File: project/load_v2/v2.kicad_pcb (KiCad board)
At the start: 2 copper layers, 118 parts, among them IC1 ATMEGA328-P, P1 12VAC, P10 relay, P2 NGUON, P3 SAC, P4 12N60C, P5 CONN_01X02, P6 button, P7 UART, P8 FAN, P9 7-seg, Q1 Q_NPN_BCE, Q2 Q_NPN_BCE, Q3 Q_NPN_BCE, SW1 reset, U1 LM7812CT, U2 LM7805CT, U3 ICL7660, U4 TL431, U5 LM324N, U6 LM324N, U7 LM7812CT, Y1 16MHz

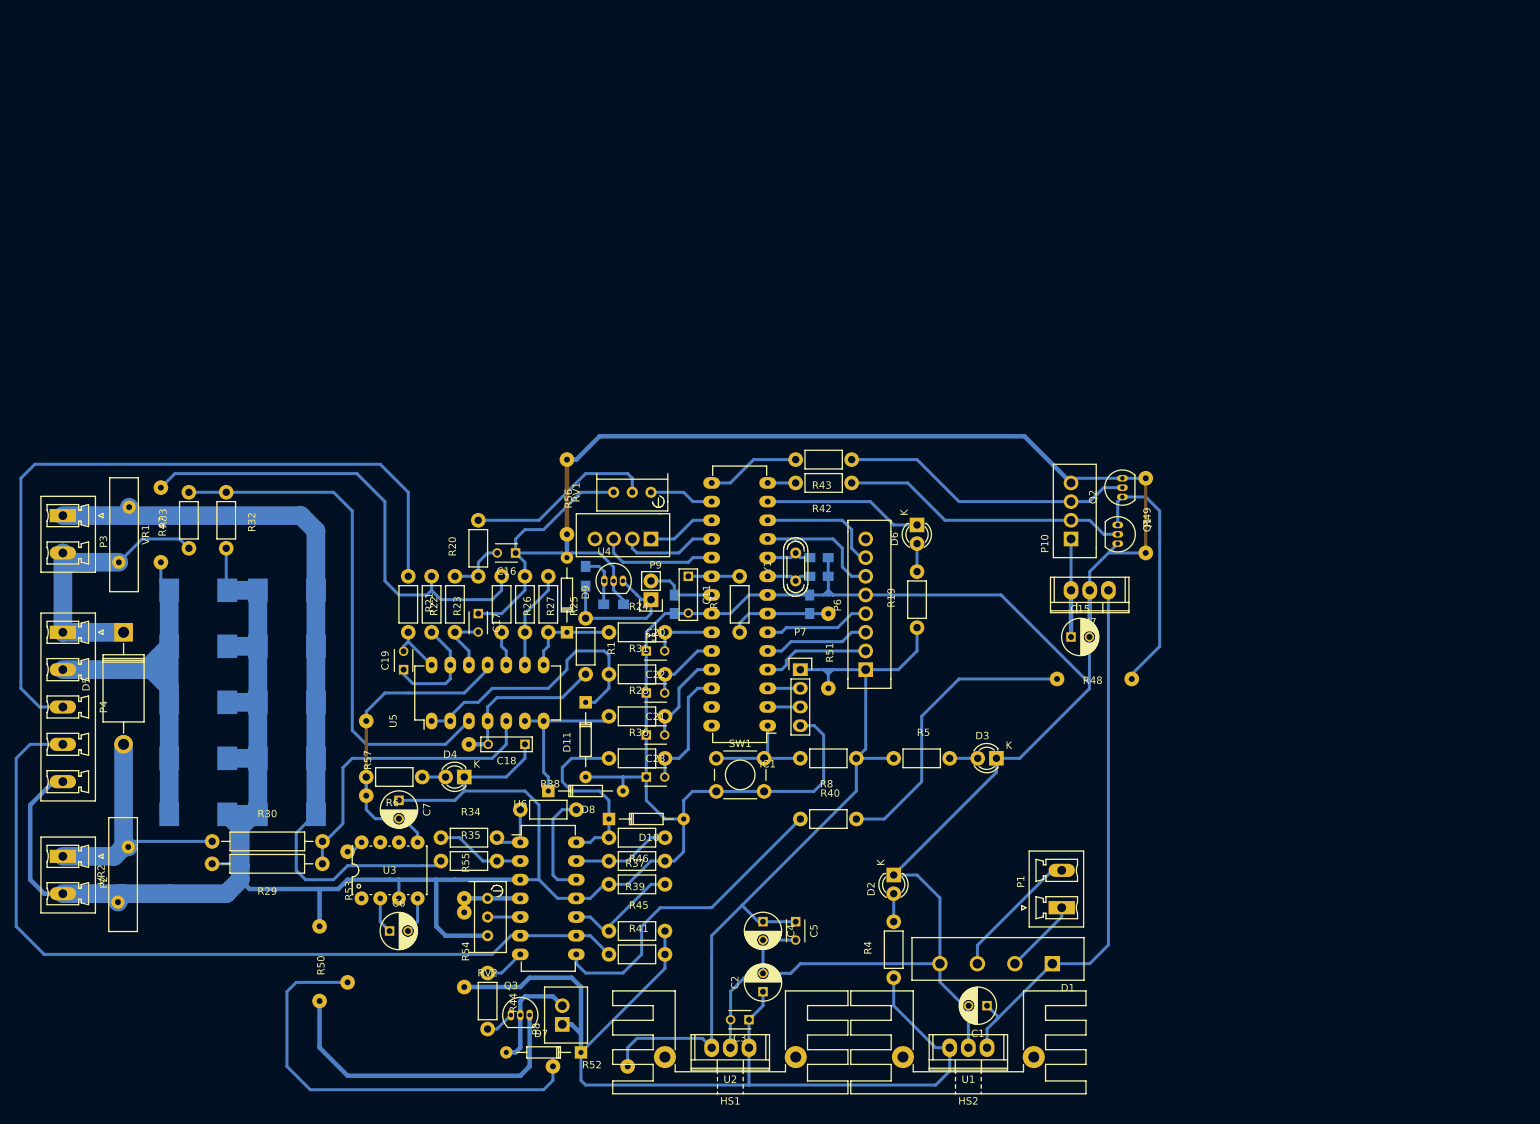
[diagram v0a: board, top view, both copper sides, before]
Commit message: schema_load_v2
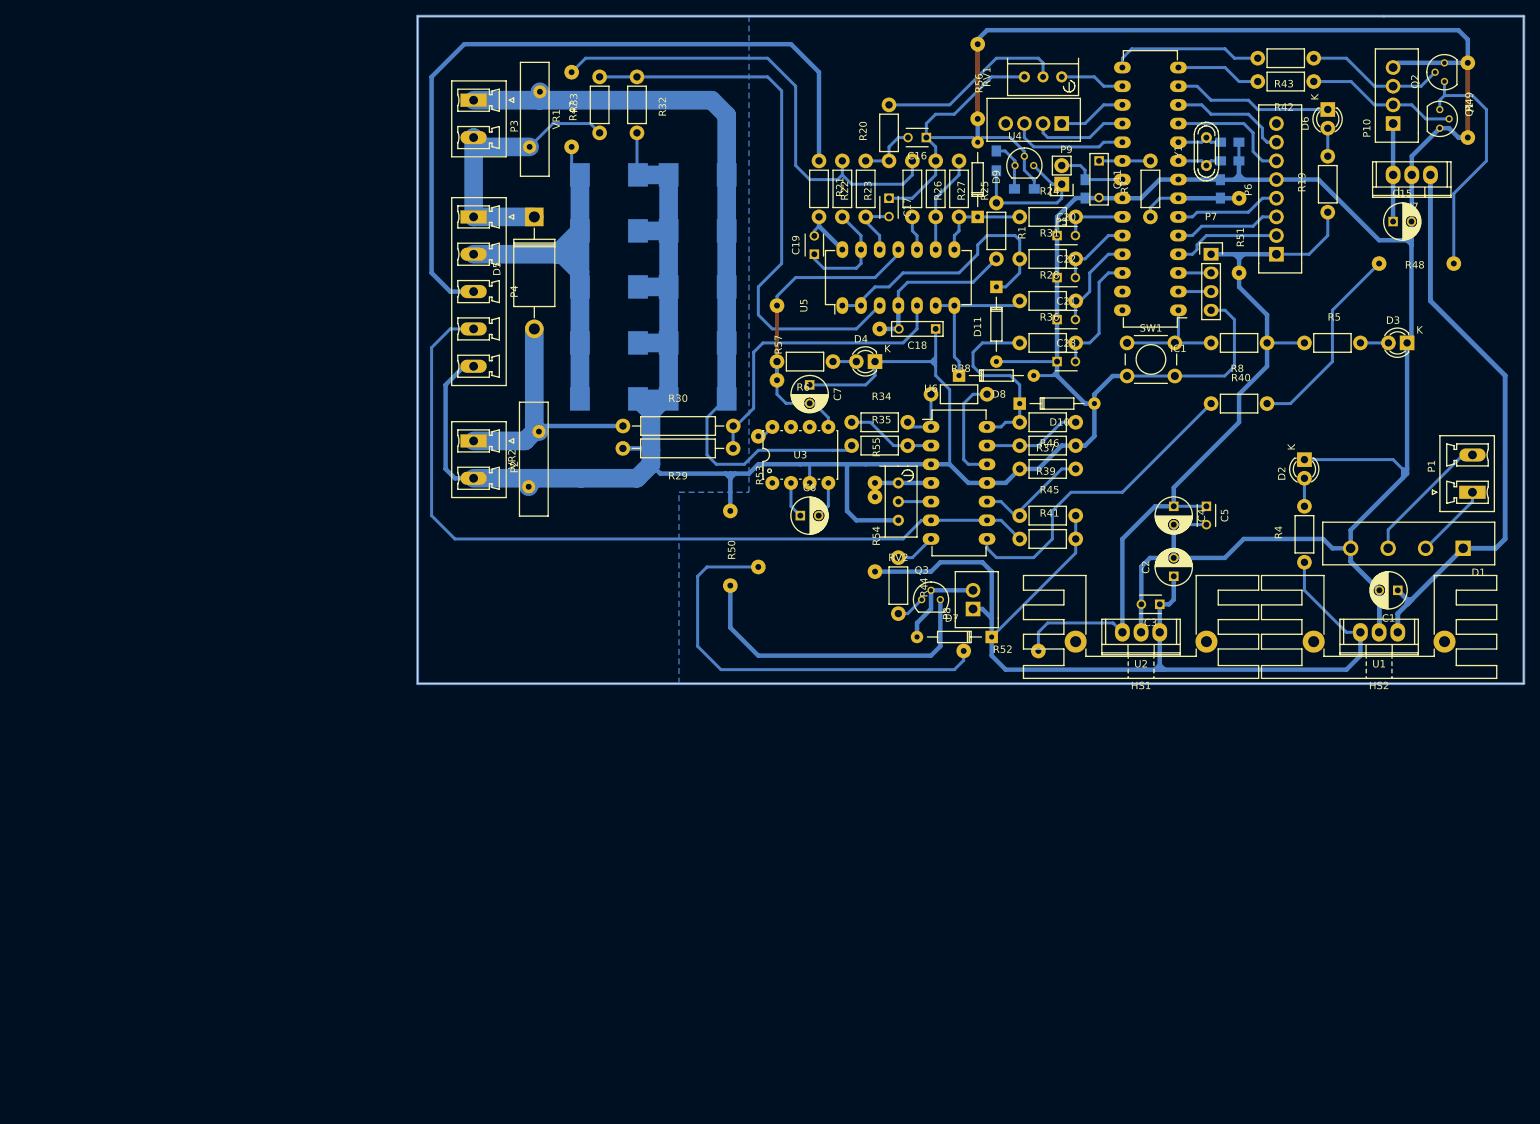
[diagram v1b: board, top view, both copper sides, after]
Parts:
- Q1, Q2, Q3, U4: footprint TO_SOT_Packages_THT:TO-92_Inline_Narrow_Oval -> TO_SOT_Packages_THT:TO-92_Molded_Narrow
- moved R42 83.3 mm to (189.9, 59.7)
- moved R43 83.3 mm to (189.9, 56.5)
- moved C17 79.5 mm to (132.1, 75.6)
- moved C18 79.5 mm to (138.4, 93.3)
- moved D10 79.5 mm to (149.9, 103.5)
- moved D7 79.5 mm to (146.1, 135.3)
- moved HS1 79.5 mm to (166.4, 135.9)
- moved P1 79.5 mm to (211.5, 115.6)
- moved R19 79.5 mm to (191.8, 77.5)
- moved R28 79.5 mm to (149.9, 89.5)
- moved R31 79.5 mm to (149.9, 83.8)
- moved R40 79.5 mm to (175.9, 103.5)
- moved R51 79.5 mm to (179.7, 85.7)
- moved R52 79.5 mm to (152.4, 137.2)
- moved C4 79.5 mm to (170.8, 117.5)
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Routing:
- net (no net): track 0.03 -> 482.6 mm
- net onS: track 40.0 -> 18.9 mm
- net 17V: track 74.7 -> 94.6 mm
- net onN: track 39.1 -> 20.5 mm
- net Net-(R40-Pad2): track 40.4 -> 27.2 mm
- net Net-(IC1-Pad15): track 12.7 -> 20.7 mm
- net Net-(IC1-Pad14): track 3.81 -> 11.6 mm
- net Net-(R32-Pad1): track 71.1 -> 76.0 mm
- net +5V: track 112.9 -> 109.1 mm
- net N-: track 703.9 -> 701.6 mm
- net Net-(D7-Pad2): track 15.0 -> 12.9 mm
- net Net-(Q3-Pad3): track 44.0 -> 42.7 mm
- net Net-(R52-Pad2): track 58.9 -> 57.6 mm
- net THa: track 115.0 -> 113.7 mm
- net +12V: track 136.3 -> 137.4 mm
- added copper zone on B.Cu, net N-
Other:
- board outline added: 150.5 x 90.8 mm
